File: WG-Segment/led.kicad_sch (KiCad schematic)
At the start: 50 parts

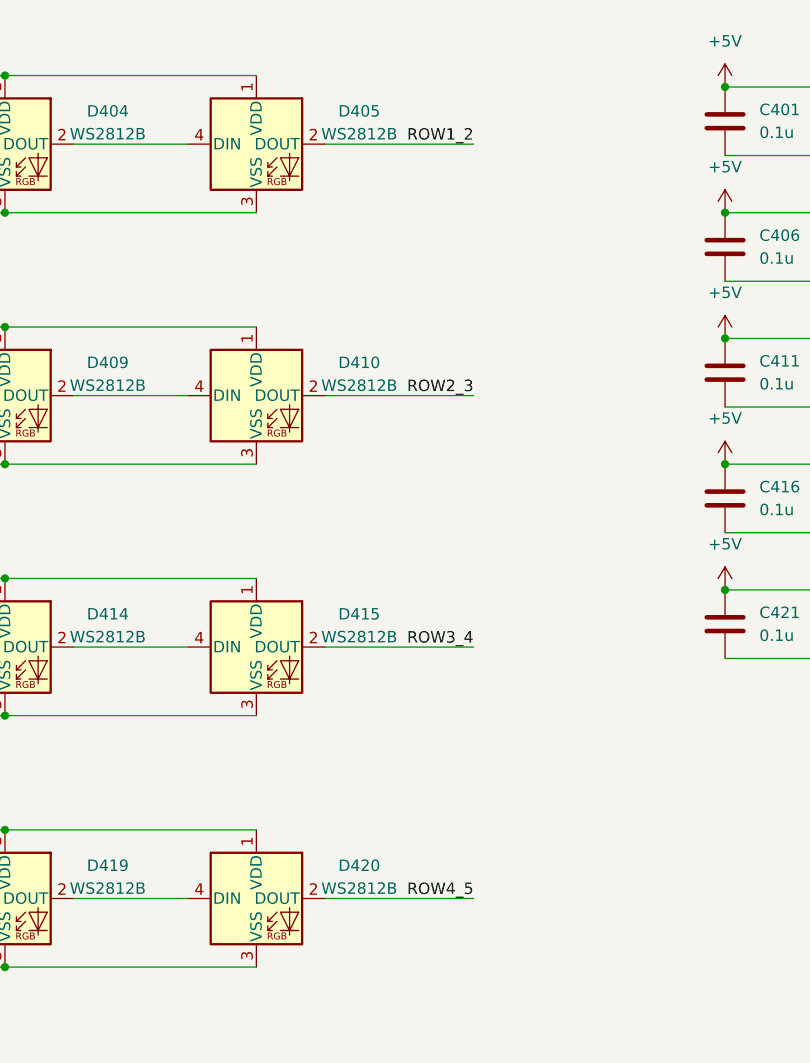
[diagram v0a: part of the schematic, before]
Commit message: Design full circuit
Still need to run ERC
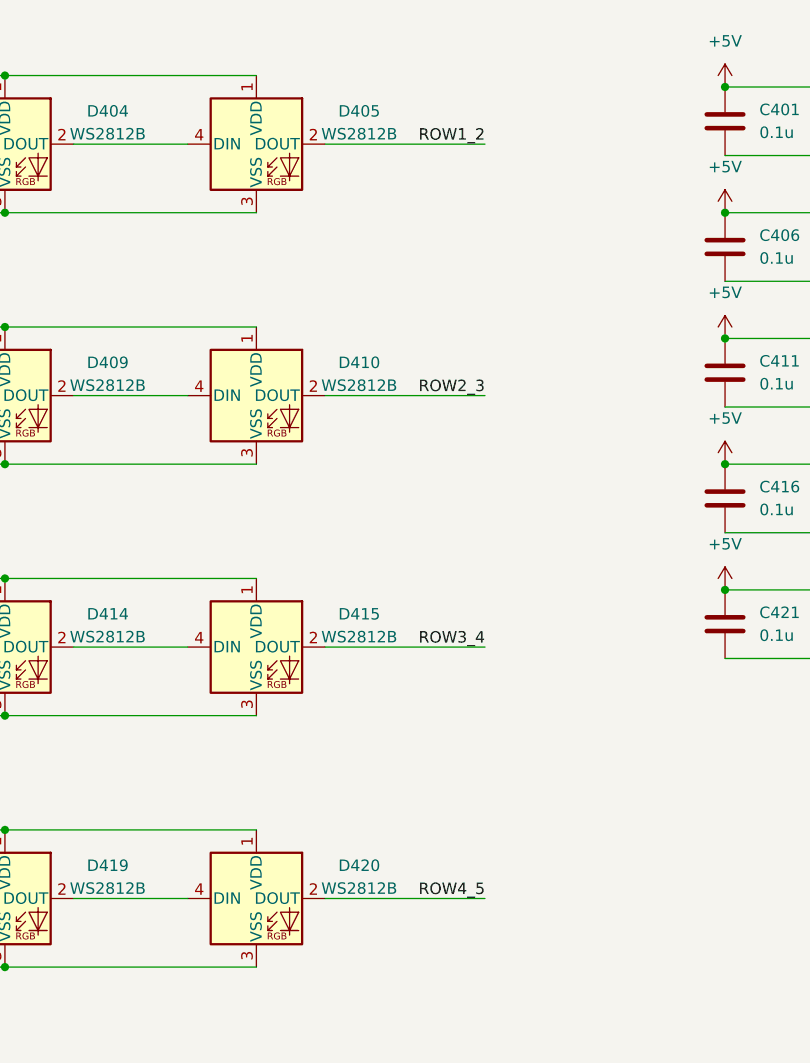
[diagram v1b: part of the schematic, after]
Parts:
- C401, C402, C403, C404, C405, C406, C407, C408, C409, C410, C411, C412, C413, C414, C415, C416, C417, C418, C419, C420, C421, C422, C423, C424, C425: footprint (none) -> Capacitor_SMD:C_0402_1005Metric_Pad0.74x0.62mm_HandSolder
- D401, D402, D403, D404, D405, D406, D407, D408, D409, D410, D411, D412, D413, D414, D415, D416, D417, D418, D419, D420, D421, D422, D423, D424, D425: Manufacturer (none) -> WORLDSEMI; Part Number (none) -> WS2812B

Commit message: Add level shifter to LED data input
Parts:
- added C426: 0.1u, Capacitor_SMD:C_0402_1005Metric_Pad0.74x0.62mm_HandSolder, symbol Device:C
- added U401: SN74LV1T34DCK, Package_TO_SOT_SMD:SOT-353_SC-70-5_Handsoldering, symbol Logic_LevelTranslator:SN74LV1T34DCK
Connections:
- net +5V: now also C426.1, U401.5 (VCC)
- net GND: now also C426.2, U401.3 (GND)
- net LED_DIN: now also U401.2 (A); no longer D401.4 (DIN)
- new net: D401.4 (DIN), U401.4 (Y)
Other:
- note added: "Level shift 3.3V->5V"
- note added: "Level shifter capacitor"
- moved on the sheet: D401, D402, D403, D404, D405, D406, D407, D408, D409, D410, D411, D412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

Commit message: Fix build issues
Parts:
- C401, C402, C403, C404, C405, C406, C407, C408, C409, C410, C411, C412, C413, C414, C415, C416, C417, C418, C419, C420, C421, C422, C423, C424, C425, C426: Desc (none) -> CAP CER 0.1uF 10V 0402
- U401: Desc (none) -> IC BUF NON-INVERT 5.5V SC70-5
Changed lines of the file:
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@@
       (effects (font (size 1.27 1.27)) hide)
     )
-    (property "Description" "CAP CER 0.1u 10V 0402" (at 234.95 130.81 0)
+    (property "Desc" "CAP CER 0.1uF 10V 0402" (at 234.95 130.81 0)
       (effects (font (size 1.27 1.27)) hide)
     )
@@
       (effects (font (size 1.27 1.27)) hide)
     )
-    (property "Description" "CAP CER 0.1u 10V 0402" (at 264.16 91.44 0)
+    (property "Desc" "CAP CER 0.1uF 10V 0402" (at 264.16 91.44 0)
       (effects (font (size 1.27 1.27)) hide)
     )
@@
       (effects (font (size 1.27 1.27)) hide)
     )
-    (property "Description" "CAP CER 0.1u 10V 0402" (at 251.46 49.53 0)
+    (property "Desc" "CAP CER 0.1uF 10V 0402" (at 251.46 49.53 0)
       (effects (font (size 1.27 1.27)) hide)
     )
@@
       (effects (font (size 1.27 1.27)) hide)
     )
-    (property "Description" "CAP CER 0.1u 10V 0402" (at 213.36 49.53 0)
+    (property "Desc" "CAP CER 0.1uF 10V 0402" (at 213.36 49.53 0)
       (effects (font (size 1.27 1.27)) hide)
     )
@@
       (effects (font (size 1.27 1.27)) hide)
     )
-    (property "Description" "IC BUF NON-INVERT 5.5V SC70-5" (at 36.83 38.1 0)
+    (property "Desc" "IC BUF NON-INVERT 5.5V SC70-5" (at 36.83 38.1 0)
       (effects (font (size 1.27 1.27)) hide)
     )
@@
       (effects (font (size 1.27 1.27)) hide)
     )
-    (property "Description" "CAP CER 0.1u 10V 0402" (at 251.46 35.56 0)
+    (property "Desc" "CAP CER 0.1uF 10V 0402" (at 251.46 35.56 0)
       (effects (font (size 1.27 1.27)) hide)
     )
@@
       (effects (font (size 1.27 1.27)) hide)
     )
-    (property "Description" "CAP CER 0.1u 10V 0402" (at 264.16 49.53 0)
+    (property "Desc" "CAP CER 0.1uF 10V 0402" (at 264.16 49.53 0)
       (effects (font (size 1.27 1.27)) hide)
     )
@@
       (effects (font (size 1.27 1.27)) hide)
     )
-    (property "Description" "CAP CER 0.1u 10V 0402" (at 226.06 63.5 0)
+    (property "Desc" "CAP CER 0.1uF 10V 0402" (at 226.06 63.5 0)
       (effects (font (size 1.27 1.27)) hide)
     )
@@
       (effects (font (size 1.27 1.27)) hide)
     )
-    (property "Description" "CAP CER 0.1u 10V 0402" (at 238.76 35.56 0)
+    (property "Desc" "CAP CER 0.1uF 10V 0402" (at 238.76 35.56 0)
       (effects (font (size 1.27 1.27)) hide)
     )
@@
       (effects (font (size 1.27 1.27)) hide)
     )
-    (property "Description" "CAP CER 0.1u 10V 0402" (at 238.76 63.5 0)
+    (property "Desc" "CAP CER 0.1uF 10V 0402" (at 238.76 63.5 0)
       (effects (font (size 1.27 1.27)) hide)
     )
@@
       (effects (font (size 1.27 1.27)) hide)
     )
-    (property "Description" "CAP CER 0.1u 10V 0402" (at 264.16 35.56 0)
+    (property "Desc" "CAP CER 0.1uF 10V 0402" (at 264.16 35.56 0)
       (effects (font (size 1.27 1.27)) hide)
     )
@@
       (effects (font (size 1.27 1.27)) hide)
     )
-    (property "Description" "CAP CER 0.1u 10V 0402" (at 251.46 91.44 0)
+    (property "Desc" "CAP CER 0.1uF 10V 0402" (at 251.46 91.44 0)
       (effects (font (size 1.27 1.27)) hide)
     )
@@
       (effects (font (size 1.27 1.27)) hide)
     )
-    (property "Description" "CAP CER 0.1u 10V 0402" (at 238.76 77.47 0)
+    (property "Desc" "CAP CER 0.1uF 10V 0402" (at 238.76 77.47 0)
       (effects (font (size 1.27 1.27)) hide)
     )
@@
       (effects (font (size 1.27 1.27)) hide)
     )
-    (property "Description" "CAP CER 0.1u 10V 0402" (at 264.16 77.47 0)
+    (property "Desc" "CAP CER 0.1uF 10V 0402" (at 264.16 77.47 0)
       (effects (font (size 1.27 1.27)) hide)
     )
@@
       (effects (font (size 1.27 1.27)) hide)
     )
-    (property "Description" "CAP CER 0.1u 10V 0402" (at 213.36 35.56 0)
+    (property "Desc" "CAP CER 0.1uF 10V 0402" (at 213.36 35.56 0)
       (effects (font (size 1.27 1.27)) hide)
     )
@@
       (effects (font (size 1.27 1.27)) hide)
     )
+    (property "Desc" "" (at 59.69 38.1 0)
+      (effects (font (size 1.27 1.27)) hide)
+    )
     (pin "3")
     (pin "4")
@@
       (effects (font (size 1.27 1.27)) hide)
     )
-    (property "Description" "CAP CER 0.1u 10V 0402" (at 251.46 63.5 0)
+    (property "Desc" "CAP CER 0.1uF 10V 0402" (at 251.46 63.5 0)
       (effects (font (size 1.27 1.27)) hide)
     )
@@
       (effects (font (size 1.27 1.27)) hide)
     )
-    (property "Description" "CAP CER 0.1u 10V 0402" (at 226.06 35.56 0)
+    (property "Desc" "CAP CER 0.1uF 10V 0402" (at 226.06 35.56 0)
       (effects (font (size 1.27 1.27)) hide)
     )
@@
       (effects (font (size 1.27 1.27)) hide)
     )
-    (property "Description" "CAP CER 0.1u 10V 0402" (at 213.36 77.47 0)
+    (property "Desc" "CAP CER 0.1uF 10V 0402" (at 213.36 77.47 0)
       (effects (font (size 1.27 1.27)) hide)
     )
@@
       (effects (font (size 1.27 1.27)) hide)
     )
-    (property "Description" "CAP CER 0.1u 10V 0402" (at 238.76 49.53 0)
+    (property "Desc" "CAP CER 0.1uF 10V 0402" (at 238.76 49.53 0)
       (effects (font (size 1.27 1.27)) hide)
     )
@@
       (effects (font (size 1.27 1.27)) hide)
     )
-    (property "Description" "CAP CER 0.1u 10V 0402" (at 251.46 77.47 0)
+    (property "Desc" "CAP CER 0.1uF 10V 0402" (at 251.46 77.47 0)
       (effects (font (size 1.27 1.27)) hide)
     )
@@
       (effects (font (size 1.27 1.27)) hide)
     )
-    (property "Description" "CAP CER 0.1u 10V 0402" (at 226.06 77.47 0)
+    (property "Desc" "CAP CER 0.1uF 10V 0402" (at 226.06 77.47 0)
       (effects (font (size 1.27 1.27)) hide)
     )
@@
       (effects (font (size 1.27 1.27)) hide)
     )
-    (property "Description" "CAP CER 0.1u 10V 0402" (at 238.76 91.44 0)
+    (property "Desc" "CAP CER 0.1uF 10V 0402" (at 238.76 91.44 0)
       (effects (font (size 1.27 1.27)) hide)
     )
@@
       (effects (font (size 1.27 1.27)) hide)
     )
-    (property "Description" "CAP CER 0.1u 10V 0402" (at 213.36 63.5 0)
+    (property "Desc" "CAP CER 0.1uF 10V 0402" (at 213.36 63.5 0)
       (effects (font (size 1.27 1.27)) hide)
     )
@@
       (effects (font (size 1.27 1.27)) hide)
     )
-    (property "Description" "CAP CER 0.1u 10V 0402" (at 226.06 91.44 0)
+    (property "Desc" "CAP CER 0.1uF 10V 0402" (at 226.06 91.44 0)
       (effects (font (size 1.27 1.27)) hide)
     )
@@
       (effects (font (size 1.27 1.27)) hide)
     )
-    (property "Description" "CAP CER 0.1u 10V 0402" (at 264.16 63.5 0)
+    (property "Desc" "CAP CER 0.1uF 10V 0402" (at 264.16 63.5 0)
       (effects (font (size 1.27 1.27)) hide)
     )
@@
       (effects (font (size 1.27 1.27)) hide)
     )
-    (property "Description" "CAP CER 0.1u 10V 0402" (at 226.06 49.53 0)
+    (property "Desc" "CAP CER 0.1uF 10V 0402" (at 226.06 49.53 0)
       (effects (font (size 1.27 1.27)) hide)
     )
@@
       (effects (font (size 1.27 1.27)) hide)
     )
-    (property "Description" "CAP CER 0.1u 10V 0402" (at 213.36 91.44 0)
-      (effects (font (size 1.27 1.27)) hide)
-    )
+    (property "Desc" "CAP CER 0.1uF 10V 0402" (at 213.36 91.44 0)
+      (effects (font (size 1.27 1.27)) hide)
+    )

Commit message: Add LCSC part numbers
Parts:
- C401, C402, C403, C404, C405, C406, C407, C408, C409, C410, C411, C412, C413, C414, C415, C416, C417, C418, C419, C420, C421, C422, C423, C424, C425, C426: LCSC Part (none) -> C1525
- U401: LCSC Part (none) -> C78541
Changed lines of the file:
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@@
+      (effects (font (size 1.27 1.27)) hide)
+    )
+    (property "LCSC Part" "C1525" (at 234.95 130.81 0)
       (effects (font (size 1.27 1.27)) hide)
     )
@@
       (effects (font (size 1.27 1.27)) hide)
     )
+    (property "LCSC Part" "C1525" (at 264.16 91.44 0)
+      (effects (font (size 1.27 1.27)) hide)
+    )
     (pin "1")
     (pin "2")
@@
       (effects (font (size 1.27 1.27)) hide)
     )
+    (property "LCSC Part" "C1525" (at 251.46 49.53 0)
+      (effects (font (size 1.27 1.27)) hide)
+    )
     (pin "1")
     (pin "2")
@@
     )
     (property "Desc" "CAP CER 0.1uF 10V 0402" (at 213.36 49.53 0)
+      (effects (font (size 1.27 1.27)) hide)
+    )
+    (property "LCSC Part" "C1525" (at 213.36 49.53 0)
       (effects (font (size 1.27 1.27)) hide)
     )
@@
       (effects (font (size 1.27 1.27)) hide)
     )
+    (property "LCSC Part" "C78541" (at 36.83 38.1 0)
+      (effects (font (size 1.27 1.27)) hide)
+    )
     (pin "1")
     (pin "2")
@@
       (effects (font (size 1.27 1.27)) hide)
     )
+    (property "LCSC Part" "C1525" (at 251.46 35.56 0)
+      (effects (font (size 1.27 1.27)) hide)
+    )
     (pin "1")
     (pin "2")
@@
       (effects (font (size 1.27 1.27)) hide)
     )
+    (property "LCSC Part" "C1525" (at 264.16 49.53 0)
+      (effects (font (size 1.27 1.27)) hide)
+    )
     (pin "1")
     (pin "2")
@@
       (effects (font (size 1.27 1.27)) hide)
     )
+    (property "LCSC Part" "C1525" (at 226.06 63.5 0)
+      (effects (font (size 1.27 1.27)) hide)
+    )
     (pin "1")
     (pin "2")
@@
     )
     (property "Desc" "CAP CER 0.1uF 10V 0402" (at 238.76 35.56 0)
+      (effects (font (size 1.27 1.27)) hide)
+    )
+    (property "LCSC Part" "C1525" (at 238.76 35.56 0)
       (effects (font (size 1.27 1.27)) hide)
     )
@@
       (effects (font (size 1.27 1.27)) hide)
     )
+    (property "LCSC Part" "C1525" (at 238.76 63.5 0)
+      (effects (font (size 1.27 1.27)) hide)
+    )
     (pin "1")
     (pin "2")
@@
       (effects (font (size 1.27 1.27)) hide)
     )
+    (property "LCSC Part" "C1525" (at 264.16 35.56 0)
+      (effects (font (size 1.27 1.27)) hide)
+    )
     (pin "1")
     (pin "2")
@@
       (effects (font (size 1.27 1.27)) hide)
     )
+    (property "LCSC Part" "C1525" (at 251.46 91.44 0)
+      (effects (font (size 1.27 1.27)) hide)
+    )
     (pin "1")
     (pin "2")
@@
     )
     (property "Desc" "CAP CER 0.1uF 10V 0402" (at 238.76 77.47 0)
+      (effects (font (size 1.27 1.27)) hide)
+    )
+    (property "LCSC Part" "C1525" (at 238.76 77.47 0)
       (effects (font (size 1.27 1.27)) hide)
     )
@@
       (effects (font (size 1.27 1.27)) hide)
     )
+    (property "LCSC Part" "C1525" (at 264.16 77.47 0)
+      (effects (font (size 1.27 1.27)) hide)
+    )
     (pin "1")
     (pin "2")
@@
       (effects (font (size 1.27 1.27)) hide)
     )
+    (property "LCSC Part" "C1525" (at 213.36 35.56 0)
+      (effects (font (size 1.27 1.27)) hide)
+    )
     (pin "1")
     (pin "2")
@@
     )
     (property "Desc" "CAP CER 0.1uF 10V 0402" (at 251.46 63.5 0)
+      (effects (font (size 1.27 1.27)) hide)
+    )
+    (property "LCSC Part" "C1525" (at 251.46 63.5 0)
       (effects (font (size 1.27 1.27)) hide)
     )
@@
       (effects (font (size 1.27 1.27)) hide)
     )
+    (property "LCSC Part" "C1525" (at 226.06 35.56 0)
+      (effects (font (size 1.27 1.27)) hide)
+    )
     (pin "1")
     (pin "2")
@@
     )
     (property "Desc" "CAP CER 0.1uF 10V 0402" (at 213.36 77.47 0)
+      (effects (font (size 1.27 1.27)) hide)
+    )
+    (property "LCSC Part" "C1525" (at 213.36 77.47 0)
       (effects (font (size 1.27 1.27)) hide)
     )
@@
       (effects (font (size 1.27 1.27)) hide)
     )
+    (property "LCSC Part" "C1525" (at 238.76 49.53 0)
+      (effects (font (size 1.27 1.27)) hide)
+    )
     (pin "1")
     (pin "2")
@@
       (effects (font (size 1.27 1.27)) hide)
     )
+    (property "LCSC Part" "C1525" (at 251.46 77.47 0)
+      (effects (font (size 1.27 1.27)) hide)
+    )
     (pin "1")
     (pin "2")
@@
       (effects (font (size 1.27 1.27)) hide)
     )
+    (property "LCSC Part" "C1525" (at 226.06 77.47 0)
+      (effects (font (size 1.27 1.27)) hide)
+    )
     (pin "1")
     (pin "2")
@@
       (effects (font (size 1.27 1.27)) hide)
     )
+    (property "LCSC Part" "C1525" (at 238.76 91.44 0)
+      (effects (font (size 1.27 1.27)) hide)
+    )
     (pin "1")
     (pin "2")
@@
       (effects (font (size 1.27 1.27)) hide)
     )
+    (property "LCSC Part" "C1525" (at 213.36 63.5 0)
+      (effects (font (size 1.27 1.27)) hide)
+    )
     (pin "1")
     (pin "2")
@@
     )
     (property "Desc" "CAP CER 0.1uF 10V 0402" (at 226.06 91.44 0)
+      (effects (font (size 1.27 1.27)) hide)
+    )
+    (property "LCSC Part" "C1525" (at 226.06 91.44 0)
       (effects (font (size 1.27 1.27)) hide)
     )
@@
       (effects (font (size 1.27 1.27)) hide)
     )
+    (property "LCSC Part" "C1525" (at 264.16 63.5 0)
+      (effects (font (size 1.27 1.27)) hide)
+    )
     (pin "1")
     (pin "2")
@@
       (effects (font (size 1.27 1.27)) hide)
     )
+    (property "LCSC Part" "C1525" (at 226.06 49.53 0)
+      (effects (font (size 1.27 1.27)) hide)
+    )
     (pin "1")
     (pin "2")
@@
       (effects (font (size 1.27 1.27)) hide)
     )
+    (property "LCSC Part" "C1525" (at 213.36 91.44 0)
+      (effects (font (size 1.27 1.27)) hide)
+    )
